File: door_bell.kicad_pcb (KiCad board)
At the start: 4 copper layers, 68.6 x 68.6 mm, 75 parts, among them J1 8-10V AC/DC, J2 Speaker, J3 SWITCH1, J4 Door panel, J5 UART, J6 JTAG, J7 BOOT, J8 MicroSD, K1 HJR 1-2C, Q1 BC847, SW1 Reset, U1 NCP1117-5v, U2 MAX98357A, U3 NCP1117-3v3, U4 DS3231M, U5 MAX3232, U6 ESP32-WROVER-B, U7 74LVC2G14

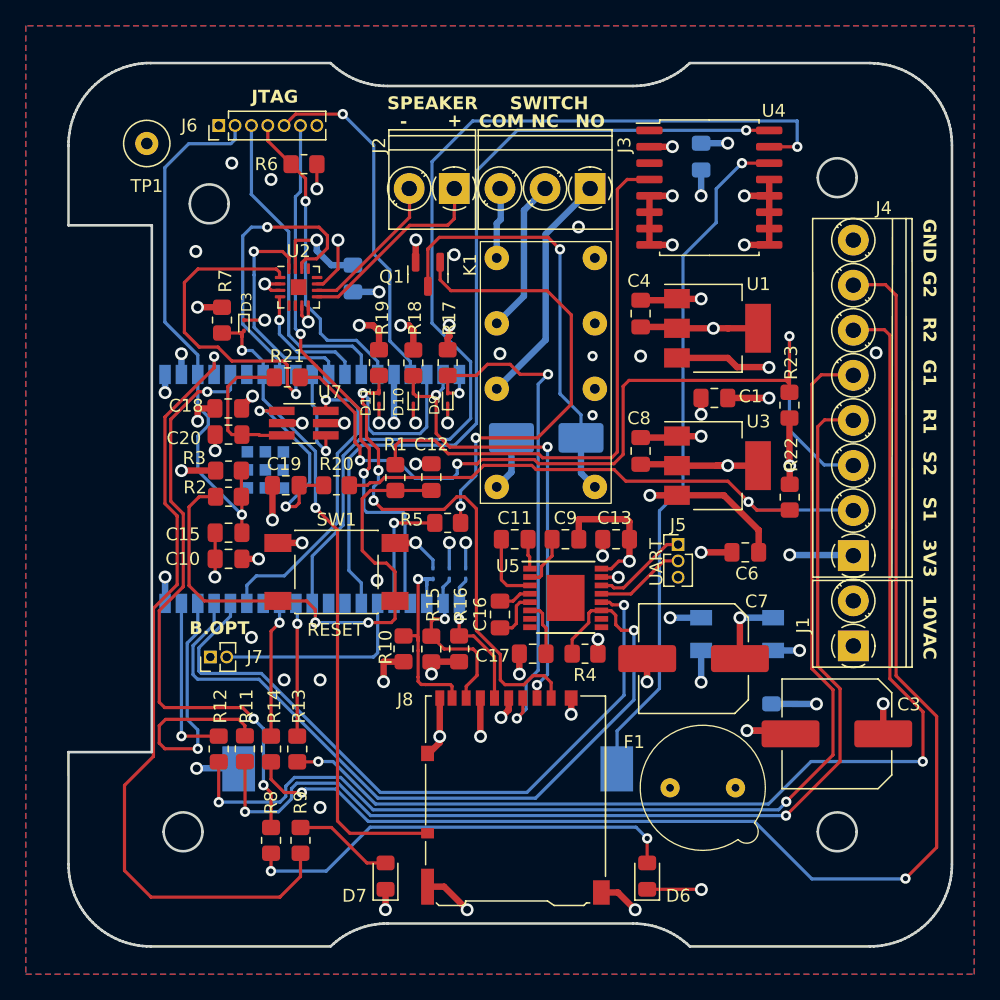
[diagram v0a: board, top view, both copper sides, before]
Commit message: Update PCB with amended board outline
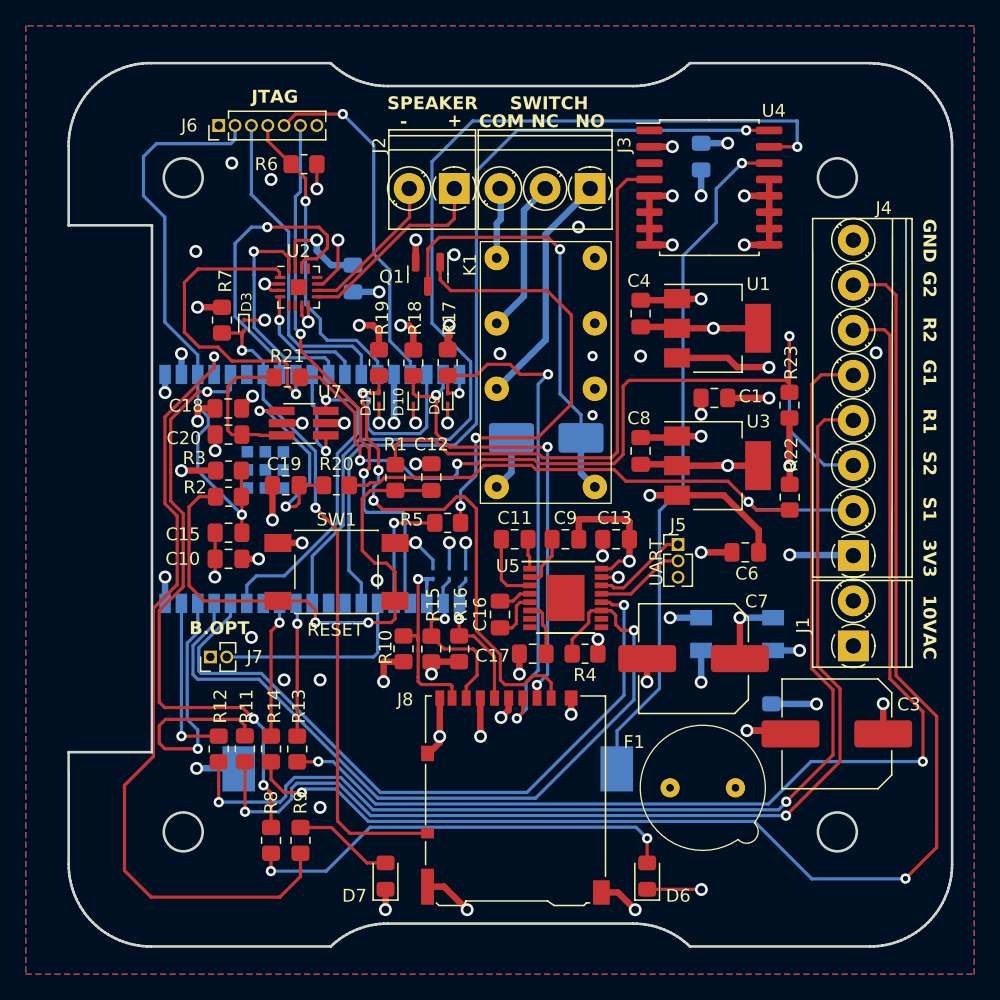
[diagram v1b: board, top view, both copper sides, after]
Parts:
- removed TP1: Ground, TestPoint:TestPoint_Loop_D3.50mm_Drill0.9mm_Beaded
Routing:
- net GND: track 545.8 -> 529.8 mm
- net +3V3: track 287.8 -> 291.6 mm
- net Net-(J6-Pin_2): track 42.4 -> 45.2 mm
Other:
- outline, holes or cut-outs redrawn

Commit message: Reset PCB and remake component placement
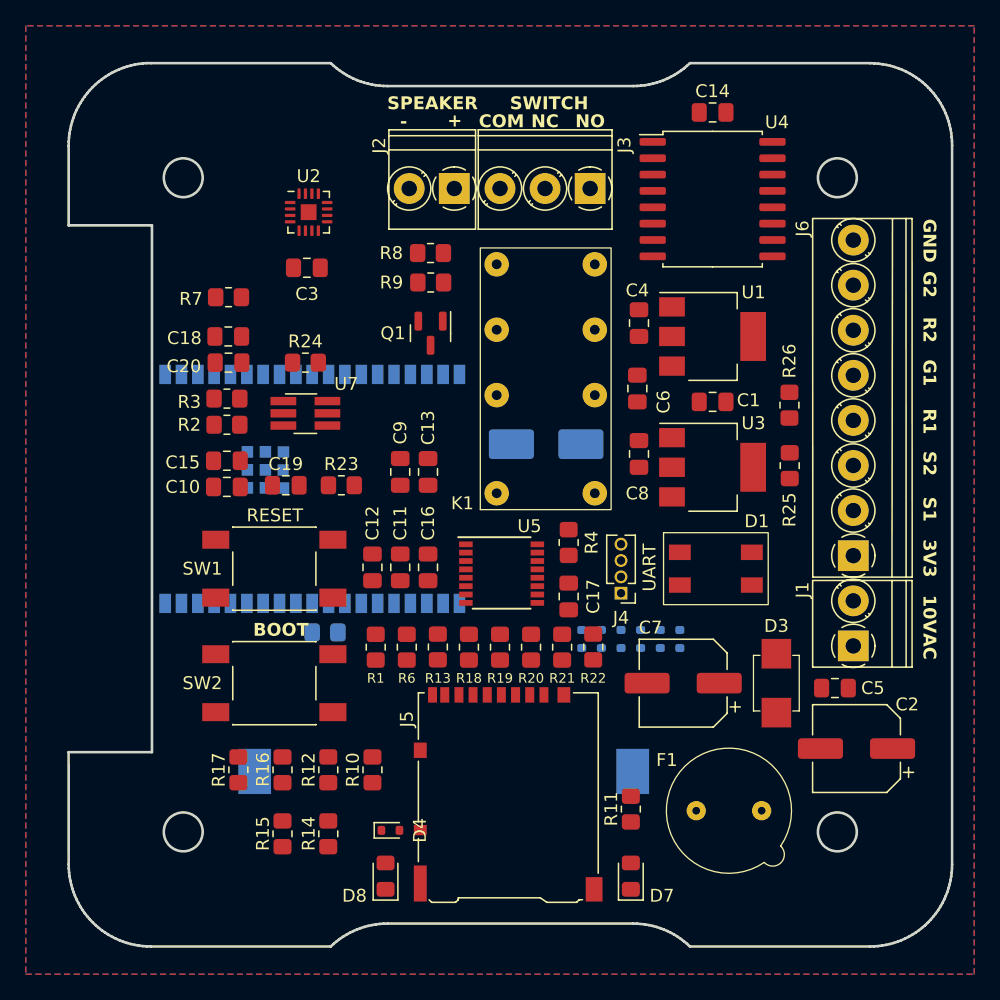
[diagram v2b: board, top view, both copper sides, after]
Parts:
- removed the D4 at (133.2, 93.3)
- removed the D8 at (135.8, 93.3)
- removed the J5 at (152.3, 91.1)
- removed the J6 at (116.6, 58.5)
- removed J7: BOOT, Connector_PinHeader_1.27mm:PinHeader_1x02_P1.27mm_Vertical
- added D3: TVSP, Diode_SMD_espena:DO-214AA-2, F.Cu at (159.9, 104.1)
- added D6: TVS, Diode_SMD:D_SOD-523, B.Cu at (146.3, 98.4)
- added D9: TVS, Diode_SMD:D_SOD-523, B.Cu at (147.8, 98.4)
- added J4: UART, Connector_PinHeader_1.27mm:PinHeader_1x04_P1.27mm_Vertical, F.Cu at (147.8, 94.9)
- added R5: 2,4k, Resistor_SMD:R_0805_2012Metric_Pad1.20x1.40mm_HandSolder, B.Cu at (124.8, 97.9)
- added R6: 2,4k, Resistor_SMD:R_0805_2012Metric_Pad1.20x1.40mm_HandSolder, F.Cu at (131.2, 99.1)
- added R7: 2,4k, Resistor_SMD:R_0805_2012Metric_Pad1.20x1.40mm_HandSolder, F.Cu at (117.3, 71.9)
- added SW2: Boot, Button_Switch_SMD_espena:SW_SPST_TL3301_6x6mm_H4.3mm, F.Cu at (120.9, 101.9)
- C14, C5, D1: moved to F.Cu
- C2: renamed from C3; footprint Capacitor_SMD:C_Elec_8x10.2 -> Capacitor_SMD:CP_Elec_6.3x9.9
- C3: renamed from C2; moved to F.Cu
- C7: footprint Capacitor_SMD:C_Elec_8x10.2 -> Capacitor_SMD:CP_Elec_6.3x9.9
- D10: renamed from D9; footprint Diode_SMD:D_SOD-923 -> Diode_SMD:D_SOD-523; moved to B.Cu
- D11: renamed from D10; footprint Diode_SMD:D_SOD-923 -> Diode_SMD:D_SOD-523; moved to B.Cu
- D12: renamed from D11; footprint Diode_SMD:D_SOD-923 -> Diode_SMD:D_SOD-523; moved to B.Cu
- D2: value S1A-13-F -> MRA4007T3G
- D4: renamed from D3; footprint Diode_SMD:D_SOD-923 -> Diode_SMD:D_SOD-523
- D5: footprint Diode_SMD:D_SOD-923 -> Diode_SMD:D_SOD-523
- R14: renamed from R11; value 75Ω -> 0Ω
- R15: renamed from R12; value 75Ω -> 0Ω
- R16: renamed from R13; value 75Ω -> 0Ω
- R17: renamed from R14; value 75Ω -> 0Ω
- R8: renamed from R5; value 10k -> 2,4k
- moved D4 40.8 mm to (129.9, 113.3), turned to 0 degrees
- moved R10 36.8 mm to (128.5, 108.6)
- moved D12 29.9 mm to (152.4, 98.4), turned to -90 degrees
- moved R11 28.0 mm to (148.6, 111.6)
- moved R22 27.6 mm to (145.7, 99.0)
- moved D11 26.8 mm to (150.9, 98.4), turned to -90 degrees
- moved R21 24.9 mm to (143.3, 99.1)
- moved D10 23.9 mm to (149.4, 98.4), turned to -90 degrees
- moved R20 23.0 mm to (140.8, 99.1)
- moved R8 21.0 mm to (133.0, 68.5)
- moved C13 15.5 mm to (132.8, 85.4), turned to -90 degrees
- moved C6 15.2 mm to (149.1, 79.0), turned to -90 degrees
- moved C9 13.9 mm to (130.7, 85.4), turned to -90 degrees
- moved R9 13.5 mm to (133.1, 70.7), turned to 180 degrees
- moved R1 13.3 mm to (128.8, 99.1), turned to 90 degrees
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- renumbered D6 to D7, D7 to D8, J8 to J5, J4 to J6, R7 to R10, R8 to R11, R9 to R12, R10 to R13, R15 to R18, R16 to R19, R17 to R20, R18 to R21, R19 to R22, R20 to R23, R21 to R24, R22 to R25, R23 to R26, R6 to R9
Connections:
- net /DIN renamed /DOUT
- D10 pad 2: Net-(D9-A2) -> /SPIMOSI
- D11 pad 2: Net-(D10-A2) -> /SPICS
- D12 pad 2: Net-(D11-A2) -> Net-(D12-A2)
- J5 pad 1: Net-(D11-A2) -> Net-(D12-A2)
- J5 pad 2: Net-(D10-A2) -> /SPICS
- J5 pad 3: Net-(D9-A2) -> /SPIMOSI
- J5 pad 5: Net-(D8-A2) -> /SPICLK
- J5 pad 7: Net-(D5-A2) -> /SPIMISO
- J5 pad 8: Net-(D4-A2) (its old number) -> Net-(D5-A2)
- R11 pad 1: Net-(U6-SENSOR_VN) -> Net-(U6-IO21)
- R12 pad 1: Net-(U6-SENSOR_VP) -> Net-(U6-IO25)
- R13 pad 2: Net-(D4-A2) (its old number) -> Net-(D5-A2)
- R18 pad 2: Net-(D5-A2) -> /SPIMISO
- R19 pad 2: Net-(D8-A2) -> /SPICLK
- R20 pad 2: Net-(D9-A2) -> /SPIMOSI
- R21 pad 2: Net-(D10-A2) -> /SPICS
- R22 pad 2: Net-(D11-A2) -> Net-(D12-A2)
- R8 pad 1: Net-(U6-IO2) -> Net-(U6-IO12)
- R9 pad 1: Net-(J6-Pin_4) -> Net-(U6-IO12)
- U6 pad 11: /BCLK -> /SPICS
- U6 pad 13: Net-(J6-Pin_3) -> /SPIMOSI
- U6 pad 14: Net-(J6-Pin_4) -> Net-(U6-IO12)
- U6 pad 16: Net-(J6-Pin_5) -> /SPIMISO
- U6 pad 17: Net-(D11-A2) -> unconnected-(U6-IO9-Pad17)
- U6 pad 18: Net-(D10-A2) -> unconnected-(U6-IO10-Pad18)
- U6 pad 19: Net-(D9-A2) -> unconnected-(U6-IO11-Pad19)
- U6 pad 20: Net-(D8-A2) -> unconnected-(U6-IO6-Pad20)
- U6 pad 21: Net-(D5-A2) -> unconnected-(U6-IO7-Pad21)
- U6 pad 22: Net-(D4-A2) (its old number) -> unconnected-(U6-IO8-Pad22)
- U6 pad 23: Net-(J6-Pin_6) -> /SPICLK
- U6 pad 24: Net-(U6-IO2) -> unconnected-(U6-IO2-Pad24)
- U6 pad 25: Net-(J7-Pin_2) -> /BCLK
- U6 pad 4: Net-(U6-SENSOR_VP) -> Net-(U6-IO36)
- U6 pad 5: Net-(U6-SENSOR_VN) -> Net-(U6-IO39)
- U7 pad 4: Net-(U6-IO25) -> Net-(U6-IO36)
- U7 pad 6: Net-(U6-IO21) -> Net-(U6-IO39)
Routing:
- net GND: track 529.8 -> 0.00 mm, vias 60 -> 0
- net +3V3: track 291.6 -> 0.00 mm, vias 19 -> 0
- net /S2_GREEN: track 105.3 -> 0.00 mm, vias 2 -> 0
- net +5V: track 96.2 -> 0.00 mm, vias 4 -> 0
- net /S2_RED: track 88.5 -> 0.00 mm, vias 2 -> 0
- net /S1_GREEN: track 87.9 -> 0.00 mm, vias 2 -> 0
- net /S1_RED: track 84.0 -> 0.00 mm, vias 2 -> 0
- net /SDA: track 78.6 -> 0.00 mm, vias 1 -> 0
- net +VDC: track 71.6 -> 0.00 mm, vias 5 -> 0
- net /~{S2_INPUT}: track 68.6 -> 0.00 mm, vias 3 -> 0
- net /SCL: track 66.3 -> 0.00 mm, vias 1 -> 0
- net Net-(U6-SENSOR_VP): track 62.0 -> 0.00 mm, vias 1 -> 0
- net Net-(U5-T1IN): track 61.3 -> 0.00 mm, vias 1 -> 0
- net Net-(U5-R1OUT): track 55.2 -> 0.00 mm, vias 1 -> 0
- net Net-(#FLG03-pwr): track 53.1 -> 0.00 mm, vias 1 -> 0
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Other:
- board text added: "BOOT"
- board text removed: "B.OPT"
- board text removed: "JTAG"

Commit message: Routing GND plane
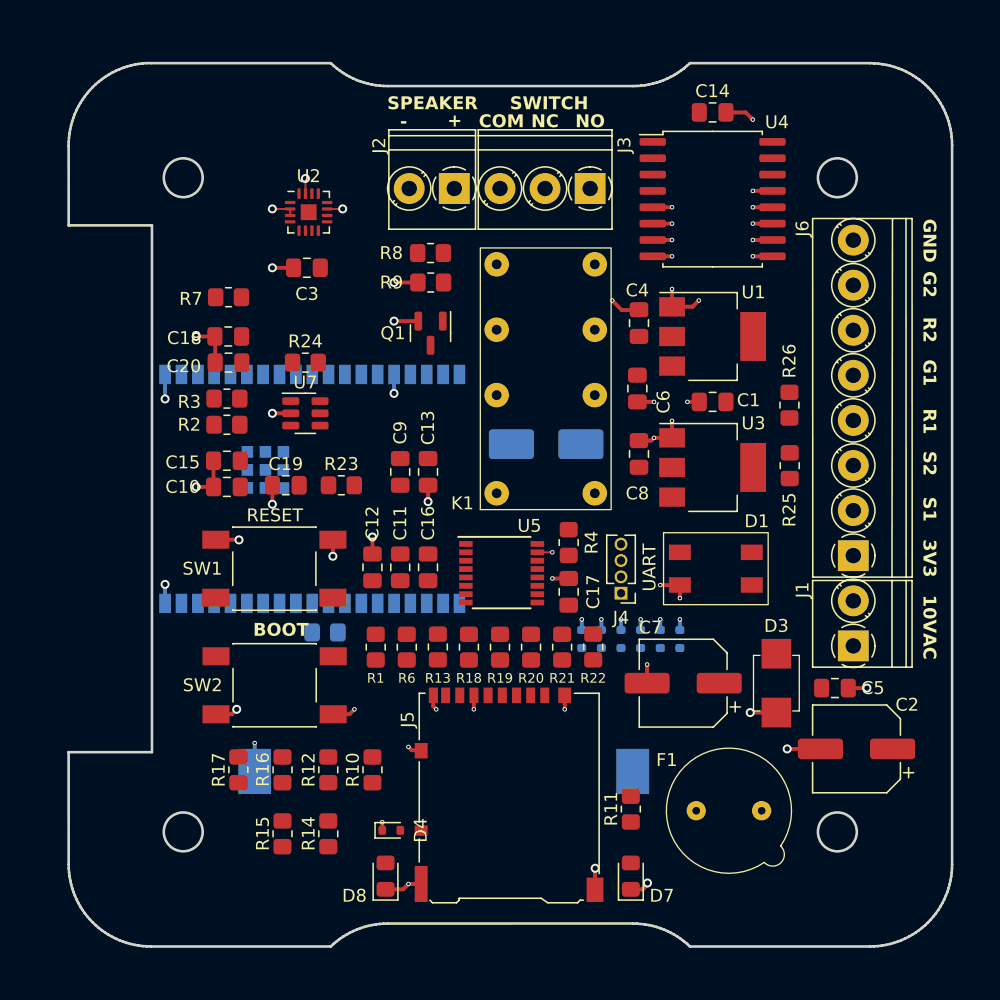
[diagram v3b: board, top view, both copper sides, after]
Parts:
- U7: footprint Package_TO_SOT_SMD:TSOT-23-6_HandSoldering -> Package_TO_SOT_SMD:TSOT-23-6
- moved C17 0.36 mm to (143.8, 94.8)
- moved SW2 0.16 mm to (120.9, 102.0)
- moved J5 0.08 mm to (139.1, 110.5)
- moved D4 0.06 mm to (130.0, 113.3)
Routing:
- net GND: track 0.00 -> 432.7 mm, vias 0 -> 59
- removed copper zone on B.Cu, net GND
- removed copper zone on F.Cu, net GND
- removed copper zone on In1.Cu, net GND

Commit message: Routing power plane
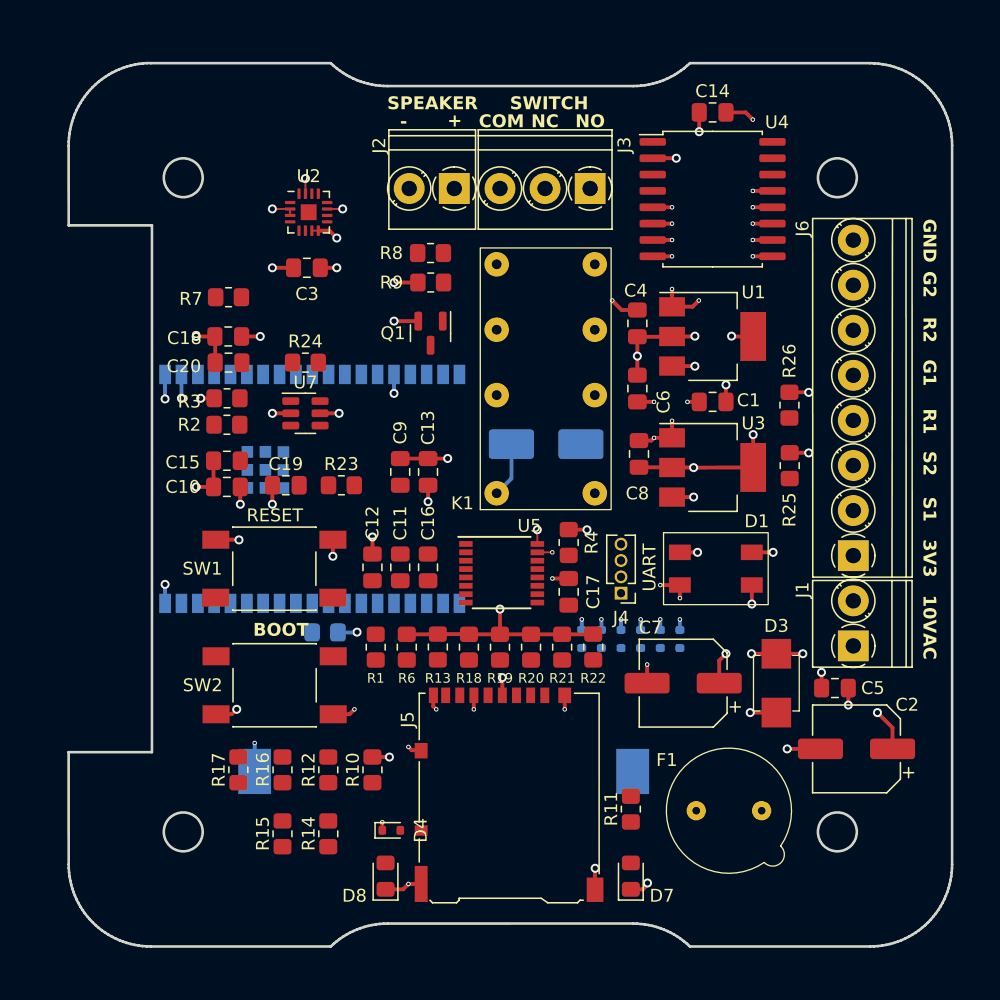
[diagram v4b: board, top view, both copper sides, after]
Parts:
- moved C4 0.13 mm to (149.1, 73.9)
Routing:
- net +3V3: track 0.00 -> 225.3 mm, vias 0 -> 18
- net +5V: track 0.00 -> 93.5 mm, vias 0 -> 6
- net +VDC: track 0.00 -> 55.4 mm, vias 0 -> 8
- net Net-(J1-Pin_2): track 0.00 -> 29.2 mm
- net Net-(D1-Pad4): track 0.00 -> 23.6 mm, vias 0 -> 1
- net Net-(J3-Pin_1): track 0.00 -> 19.1 mm
- net Net-(J1-Pin_1): track 0.00 -> 15.1 mm, vias 0 -> 1
- net Net-(J3-Pin_2): track 0.00 -> 13.5 mm
- net Net-(J3-Pin_3): track 0.00 -> 5.99 mm
- net GND: track 432.7 -> 429.8 mm
- removed copper zone on In2.Cu, net +3V3

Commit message: Routing complete
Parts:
- moved BT1 0.09 mm to (134.1, 108.7)
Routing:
- net /S2_GREEN: track 0.00 -> 86.5 mm, vias 0 -> 1
- net /S2_RED: track 0.00 -> 80.1 mm, vias 0 -> 1
- net /S1_GREEN: track 0.00 -> 75.1 mm, vias 0 -> 1
- net /S1_RED: track 0.00 -> 67.7 mm, vias 0 -> 1
- net /SCL: track 0.00 -> 64.0 mm, vias 0 -> 2
- net /SPICS: track 0.00 -> 58.2 mm, vias 0 -> 3
- net /SDA: track 0.00 -> 56.1 mm, vias 0 -> 1
- net Net-(#FLG03-pwr): track 0.00 -> 56.0 mm, vias 0 -> 1
- net Net-(U4-~{RST}): track 0.00 -> 53.1 mm, vias 0 -> 2
- net /~{S2_INPUT}: track 0.00 -> 48.9 mm
- net /BCLK: track 0.00 -> 46.9 mm, vias 0 -> 1
- net /SPIMOSI: track 0.00 -> 46.3 mm, vias 0 -> 2
- net Net-(U6-IO21): track 0.00 -> 46.0 mm, vias 0 -> 1
- net /~{S1_INPUT}: track 0.00 -> 44.6 mm
- net Net-(D4-A2): track 0.00 -> 42.8 mm, vias 0 -> 1
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- added copper zone on In2.Cu, net +3V3
- added copper zone on In1.Cu, net GND

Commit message: Revision 1.1 plotted and sent to factory
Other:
- board text added: "DUAL BUTTON DOORBELL"
- board text added: "www.espenandersen.no"

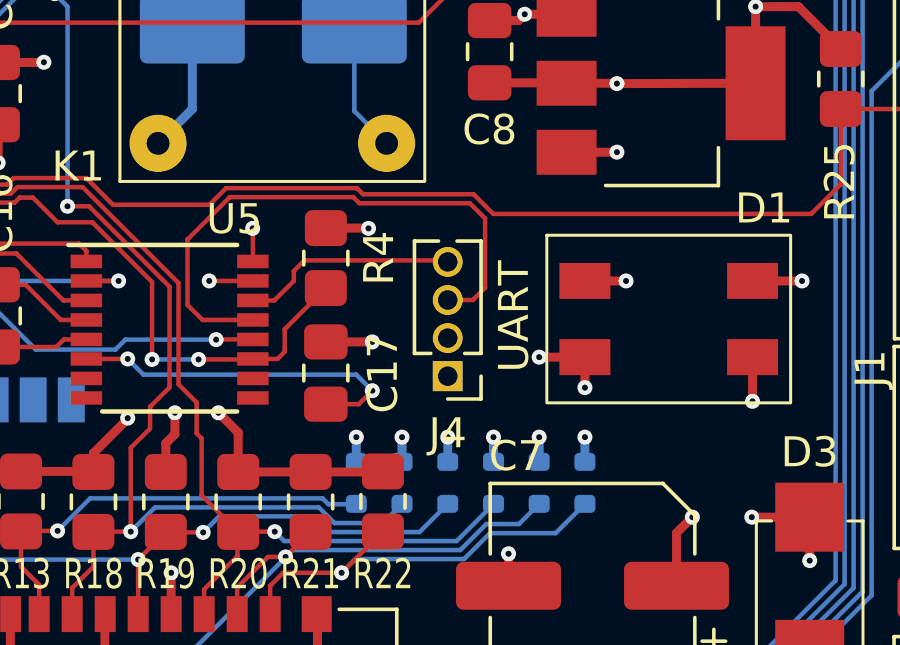
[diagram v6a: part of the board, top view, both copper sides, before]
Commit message: Empty position in UART header to block connector if accidentially reversed
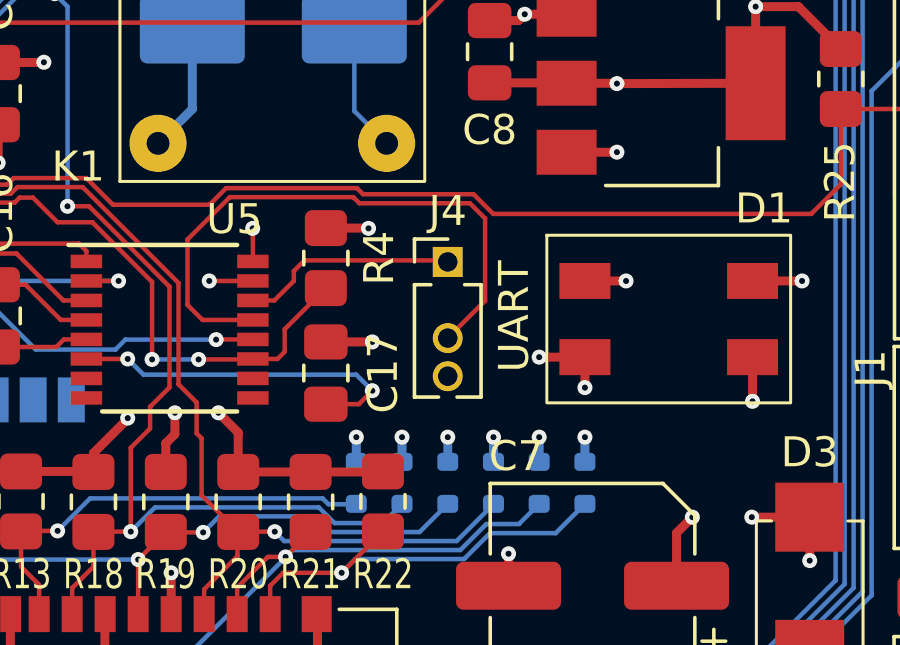
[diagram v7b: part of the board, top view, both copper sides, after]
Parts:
- J4: footprint Connector_PinHeader_1.27mm:PinHeader_1x04_P1.27mm_Vertical -> Connector_PinHeader_1.27mm_espena:PinHeader_1x04_P1.27mm_Vertical_without_pin2
- moved J4 3.81 mm to (147.8, 91.1), turned to 0 degrees
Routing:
- net Net-(J4-Pin_3): track 19.1 -> 19.9 mm
